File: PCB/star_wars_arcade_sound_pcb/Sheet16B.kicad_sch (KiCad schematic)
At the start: 0 parts

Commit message: Finished schematic
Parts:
- added A_3: LM556, symbol atari:LM556
- added B_2, C_3: TL084, symbol atari:TL084
- added B_3: R5106, symbol atari:R5106
- added C43, C45, C54, C55, C59, C60: .1uf, symbol Device:C
- added C44: .01uf, symbol Device:C
- added C46, C48, C49, C50, C56, C57, C58: .0027uf, symbol Device:C
- added C47, C53: 100uf 50v, symbol Device:C_Polarized_US
- added C51: .47uf, symbol Device:C
- added C52: 10uf 35v, symbol Device:C_Polarized_US
- added Q4: 2N3904, Package_TO_SOT_THT:TO-92_Inline, symbol Transistor_BJT:2N3904
- added R31, R32: 560k, symbol Device:R_US
- added R33, R34: 4.7k, symbol Device:R_US
- added R35, R51, R56: 2.2k, symbol Device:R_US
- added R36: 15, symbol Device:R_US
- added R37: 10k, symbol Device:R_US
- added R38: 470, symbol Device:R_US
- added R39, R40, R42, R46, R47: 12k, symbol Device:R_US
- added R41: 68k, symbol Device:R_US
- added R43: 1.5k, symbol Device:R_US
- added R44: 100, symbol Device:R_US
- added R45: 470k, symbol Device:R_US
- added R48, R49, R52, R53: 22k, symbol Device:R_US
- added R50, R54, R55: 47k, symbol Device:R_US
- added TP10, TP8, TP9: tp_2_pin, symbol atari:tp_2_pin
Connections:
- new net: B_2.1, B_2.2 (-), C56.2, C57.2, R48.1, R52.1
- new net: B_2.6 (-), R48.2, R49.2, R50.1
- new net: Q4.2 (B), R37.2
- new net: Q4.3 (C), R36.1
- new net: B_2.9 (-), R52.2, R55.1
- new net: B_2.8, R55.2, R56.1, TP10.1, TP10.2
- new net: R41.1, R42.2, R43.1
- new net: B_3.5 (VBB), C52.1, R43.2
- new net: A_3.2 (THR), A_3.6 (TR), B_2.12 (+), C43.2, R32.1
- new net: A_3.1 (DIS), R31.1, R32.2
- new net: B_2.10 (+), R53.2, R54.2
- new net: C50.2, C_3.12 (+), R40.2
- new net: B_2.7, R50.2, R51.1, TP9.1, TP9.2
- new net: B_3.8 (VDD), C53.1, C54.1, R44.1
- new net: C56.1, C57.1, R46.2, R47.1
- new net: B_2.3 (+), C58.2, R47.2
- new net: C48.1, C49.1, R39.2, R40.1
- new net: A_3.3 (CV), C44.2
- new net: A_3.13 (DIS), R33.1, R34.2
- new net: B_3.4 (OUT), C55.1
- new net: C55.2, C_3.10 (+), R45.2
- new net: A_3.11 (CV), C47.1
- new net: A_3.12 (THR), A_3.8 (TR), C46.2, R34.1
- new net: C47.2, R35.2, R36.2, R38.2
- new net: B_3.6 (IN), C51.2, R41.2
- new net: B_2.13 (-), B_2.14, R35.1
- new net: C_3.8, C_3.9 (-), R46.1
- new net +12V: A_3.10 (R), A_3.14 (VCC), A_3.4 (R), B_2.4 (V+), C45.1, C59.1, R31.2, R33.2, R44.2
- new net -5V: B_2.11 (V-), C60.1
- new net AUD: C48.2, C49.2, C51.1, C_3.13 (-), C_3.14, R49.1, R53.1, TP8.1, TP8.2
- new net GND: A_3.7 (GND), B_2.5 (+), B_3.2 (VSS), B_3.7 (SYNC), C43.1, C44.1, C45.2, C46.1, C50.1, C52.2, C53.2, C54.2, C58.1, C59.2, C60.2, Q4.1 (E), R38.1, R42.1, R45.1, R54.1
- new net LEFT_AUDIO: R51.2
- new net PA3: R37.1
- new net RCK: A_3.9 (Q), B_3.1 (CLK)
- new net RIGHT_AUDIO: R56.2
- new net SUM: R39.1
- no-connect marks 0 -> 2
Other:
- note added: "DELAY"
- note added: "DELAY CLOCK"
- note added: "FILTER"
- note added: "OUTPUT AND SUMMING AMPLIFIERS"

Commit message: Began PCB layout
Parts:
- B_3: footprint (none) -> atari:DIP8
- Q4: footprint Package_TO_SOT_THT:TO-92_Inline -> (none)
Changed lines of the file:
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@@
       (effects (font (size 1.27 1.27)) (justify left))
     )
-    (property "Footprint" "Package_TO_SOT_THT:TO-92_Inline" (id 2) (at 220.345 218.44 0)
+    (property "Footprint" "" (id 2) (at 220.345 218.44 0)
       (effects (font (size 1.27 1.27) italic) (justify left) hide)
     )
@@
       (effects (font (size 1.27 1.27)) (justify left))
     )
-    (property "Footprint" "" (id 2) (at 135.255 71.755 0)
-      (effects (font (size 1.27 1.27)) hide)
-    )
+    (property "Footprint" "atari:DIP8" (id 2) (at 135.255 71.755 0)
+      (effects (font (size 1.27 1.27)) hide)
+    )

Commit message: ICs placed
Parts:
- A_3, B_2, C_3: footprint (none) -> atari:DIP14
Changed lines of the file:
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@@
       (effects (font (size 1.27 1.27)) (justify left))
     )
-    (property "Footprint" "" (id 2) (at 224.155 60.325 0)
+    (property "Footprint" "atari:DIP14" (id 2) (at 224.155 60.325 0)
       (effects (font (size 1.27 1.27)) hide)
     )
@@
     (property "Reference" "A_3" (id 0) (at 167.64 160.655 0))
     (property "Value" "LM556" (id 1) (at 167.64 162.56 0))
-    (property "Footprint" "" (id 2) (at 167.64 161.29 0)
+    (property "Footprint" "atari:DIP14" (id 2) (at 167.64 161.29 0)
       (effects (font (size 1.27 1.27)) hide)
     )
@@
     (property "Reference" "B_2" (id 0) (at 290.83 92.71 0))
     (property "Value" "TL084" (id 1) (at 290.83 94.615 0))
-    (property "Footprint" "" (id 2) (at 291.465 95.885 0)
+    (property "Footprint" "atari:DIP14" (id 2) (at 291.465 95.885 0)
       (effects (font (size 1.27 1.27)) hide)
     )
@@
     (property "Reference" "B_2" (id 0) (at 290.83 64.77 0))
     (property "Value" "TL084" (id 1) (at 290.83 66.675 0))
-    (property "Footprint" "" (id 2) (at 291.465 67.945 0)
+    (property "Footprint" "atari:DIP14" (id 2) (at 291.465 67.945 0)
       (effects (font (size 1.27 1.27)) hide)
     )
@@
     (property "Reference" "A_3" (id 0) (at 233.68 160.02 0))
     (property "Value" "LM556" (id 1) (at 233.68 161.925 0))
-    (property "Footprint" "" (id 2) (at 233.68 161.29 0)
+    (property "Footprint" "atari:DIP14" (id 2) (at 233.68 161.29 0)
       (effects (font (size 1.27 1.27)) hide)
     )
@@
     (property "Reference" "B_2" (id 0) (at 223.52 62.23 0))
     (property "Value" "TL084" (id 1) (at 223.52 64.135 0))
-    (property "Footprint" "" (id 2) (at 224.155 65.405 0)
+    (property "Footprint" "atari:DIP14" (id 2) (at 224.155 65.405 0)
       (effects (font (size 1.27 1.27)) hide)
     )
@@
     (property "Reference" "C_3" (id 0) (at 67.945 67.31 0))
     (property "Value" "TL084" (id 1) (at 67.945 69.215 0))
-    (property "Footprint" "" (id 2) (at 68.58 70.485 0)
+    (property "Footprint" "atari:DIP14" (id 2) (at 68.58 70.485 0)
       (effects (font (size 1.27 1.27)) hide)
     )
@@
     (property "Reference" "B_2" (id 0) (at 190.5 198.12 0))
     (property "Value" "TL084" (id 1) (at 190.5 200.025 0))
-    (property "Footprint" "" (id 2) (at 191.135 201.93 0)
+    (property "Footprint" "atari:DIP14" (id 2) (at 191.135 201.93 0)
       (effects (font (size 1.27 1.27)) hide)
     )
@@
     (property "Reference" "C_3" (id 0) (at 177.165 66.675 0))
     (property "Value" "TL084" (id 1) (at 177.165 64.77 0))
-    (property "Footprint" "" (id 2) (at 177.8 67.945 0)
-      (effects (font (size 1.27 1.27)) hide)
-    )
+    (property "Footprint" "atari:DIP14" (id 2) (at 177.8 67.945 0)
+      (effects (font (size 1.27 1.27)) hide)
+    )

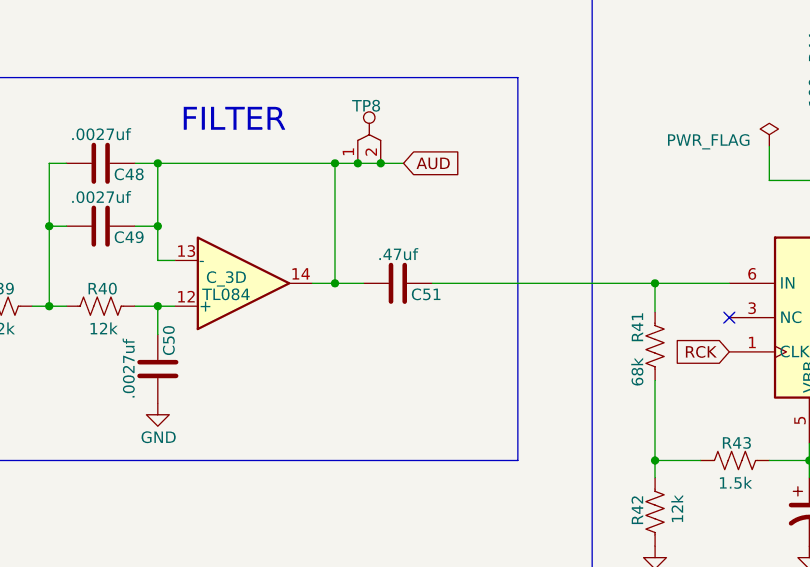
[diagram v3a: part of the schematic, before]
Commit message: Placed all components
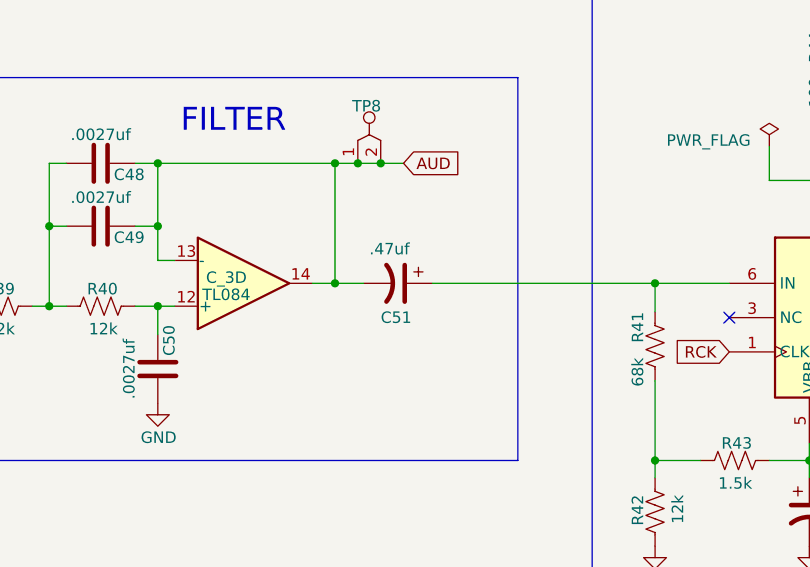
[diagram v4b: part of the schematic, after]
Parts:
- removed C51: .47uf, symbol Device:C
- added C51: .47uf, atari:MedCap1, symbol Device:C_Polarized_US
- C43, C44, C45, C46, C48, C49, C50, C54, C55, C56, C57, C58, C59, C60, R31, R32, R33, R34, R35, R36, R37, R38, R39, R40, R41, R42, R43, R44, R45, R46, R47, R48, R49, R50, R51, R52, R53, R54, R55, R56: footprint (none) -> atari:GenericComp
- C47, C53: footprint (none) -> atari:LargeCap1
- C52: footprint (none) -> atari:MedCap1
- Q4: footprint (none) -> atari:GenericTrans
- TP10, TP8, TP9: footprint (none) -> atari:TEST_POINT
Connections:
- net AUD: now also C51.2
- net at B_3.6 (IN), R41.2: now also C51.1

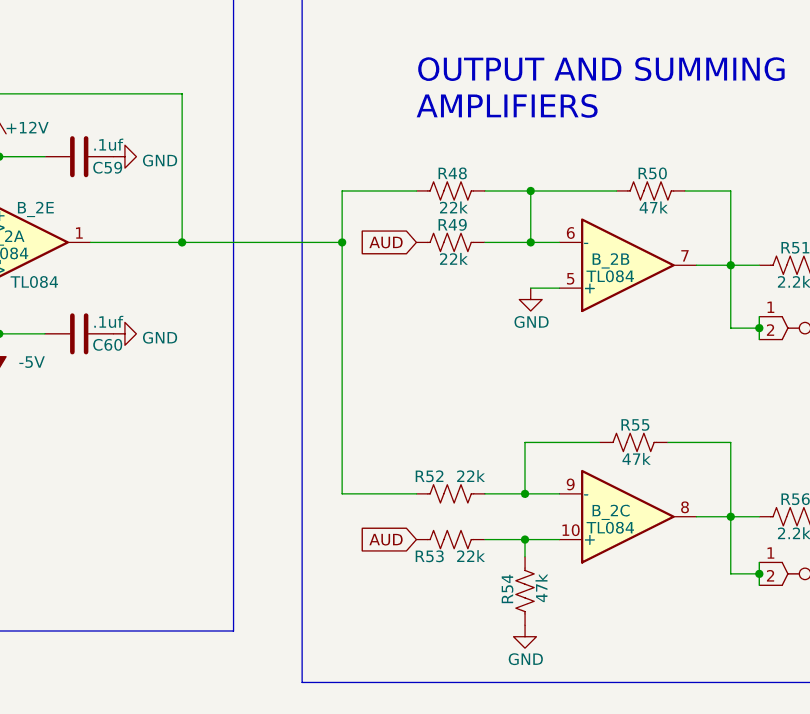
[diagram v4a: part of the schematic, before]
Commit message: Ground plane and mounting holes remain
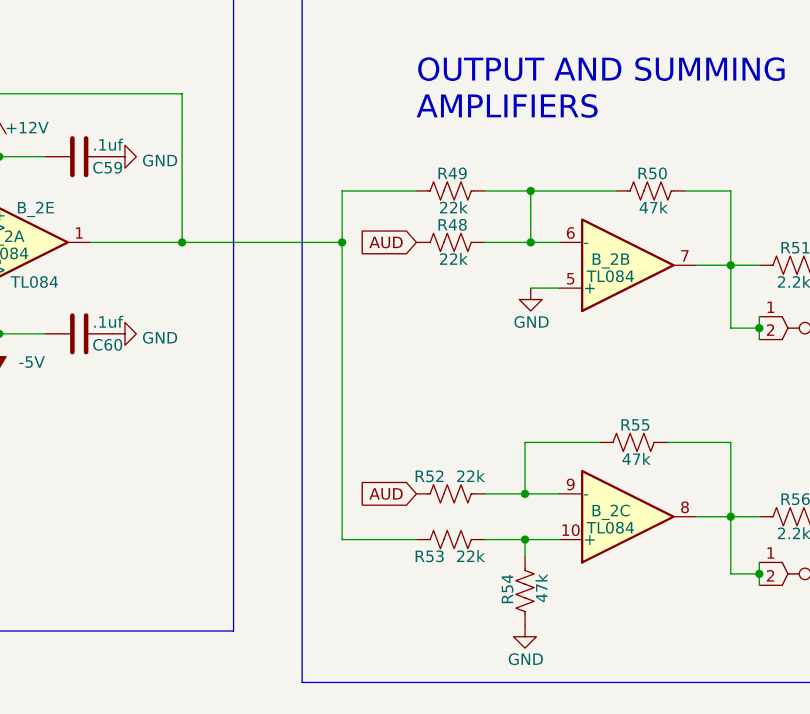
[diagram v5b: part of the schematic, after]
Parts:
- renumbered R49 to R48, R48 to R49
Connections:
- net AUD: now also R52.1; no longer R53.1
- net at B_2.1, B_2.2 (-), C56.2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: now also R53.1; no longer R52.1
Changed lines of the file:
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@@
     (stroke (width 0) (type default) (color 0 0 0 0))
   )
-  (wire (pts (xy 260.985 62.865) (xy 260.985 90.805))
+  (wire (pts (xy 260.985 62.865) (xy 260.985 95.885))
     (stroke (width 0) (type default) (color 0 0 0 0))
   )
@@
     (stroke (width 0) (type default) (color 0 0 0 0))
   )
-  (wire (pts (xy 260.985 90.805) (xy 269.24 90.805))
-    (stroke (width 0) (type default) (color 0 0 0 0))
-  )
   (wire (pts (xy 229.87 199.39) (xy 229.87 201.295))
     (stroke (width 0) (type default) (color 0 0 0 0))
@@
   )
   (wire (pts (xy 172.085 149.225) (xy 163.195 149.225))
+    (stroke (width 0) (type default) (color 0 0 0 0))
+  )
+  (wire (pts (xy 269.24 95.885) (xy 260.985 95.885))
     (stroke (width 0) (type default) (color 0 0 0 0))
   )
@@
     )
   )
-  (global_label "AUD" (shape input) (at 269.24 95.885 180) (fields_autoplaced)
+  (global_label "AUD" (shape input) (at 269.24 90.805 180) (fields_autoplaced)
     (effects (font (size 1.27 1.27)) (justify right))
-    (property "Intersheet References" "${INTERSHEET_REFS}" (id 0) (at 263.1379 95.8056 0)
+    (property "Intersheet References" "${INTERSHEET_REFS}" (id 0) (at 263.1379 90.7256 0)
       (effects (font (size 1.27 1.27)) (justify right) hide)
     )
@@
   (symbol (lib_id "Device:R_US") (at 273.05 57.15 90) (unit 1)
     (in_bom yes) (on_board yes)
-    (property "Reference" "R48" (id 0) (at 274.955 55.245 90)
+    (property "Reference" "R49" (id 0) (at 274.955 55.245 90)
       (effects (font (size 1.27 1.27)) (justify left))
     )
@@
   (symbol (lib_id "Device:R_US") (at 273.05 62.865 90) (unit 1)
     (in_bom yes) (on_board yes)
-    (property "Reference" "R49" (id 0) (at 274.955 60.96 90)
-      (effects (font (size 1.27 1.27)) (justify left))
-    )
+    (property "Reference" "R48" (id 0) (at 274.955 60.96 90)
+      (effects (font (size 1.27 1.27)) (justify left))
+    )

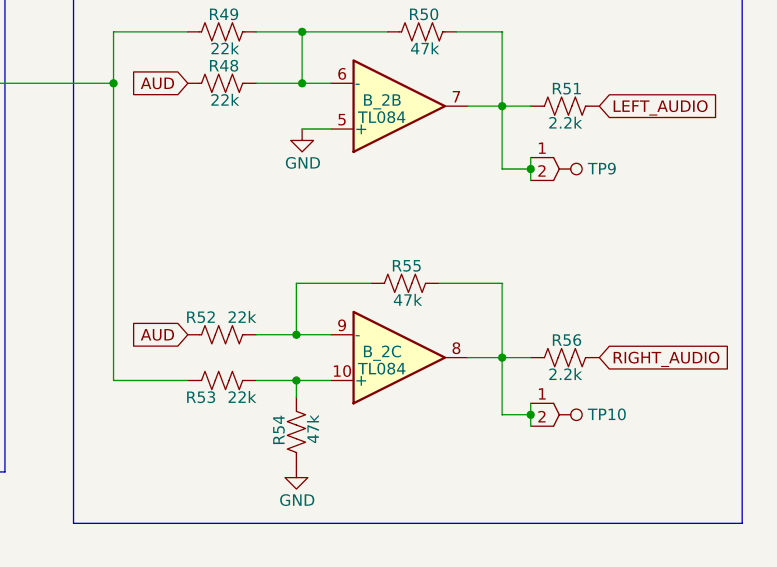
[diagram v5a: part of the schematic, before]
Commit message: Bottom keep out areas remain
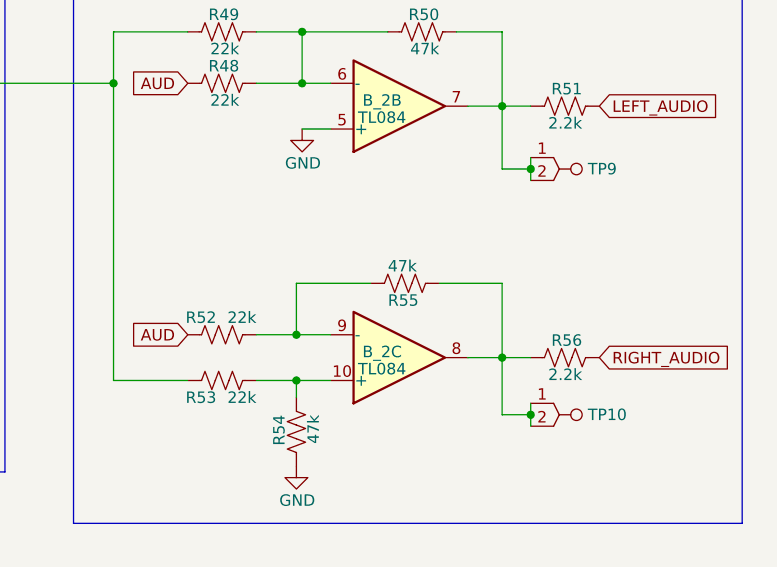
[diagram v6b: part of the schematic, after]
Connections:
- net at B_2.9 (-), R52.2: now also R55.2; no longer R55.1
- net at B_2.8, R56.1, TP10.1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: now also R55.1; no longer R55.2
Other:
- moved on the sheet: R55
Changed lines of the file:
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@@
     (pin "3")
   )
-  (symbol (lib_id "Device:R_US") (at 293.37 85.09 90) (unit 1)
+  (symbol (lib_id "Device:R_US") (at 293.37 85.09 270) (unit 1)
     (in_bom yes) (on_board yes)
-    (property "Reference" "R55" (id 0) (at 295.275 83.185 90)
+    (property "Reference" "R55" (id 0) (at 291.465 86.995 90)
       (effects (font (size 1.27 1.27)) (justify left))
     )
-    (property "Value" "47k" (id 1) (at 295.275 86.995 90)
+    (property "Value" "47k" (id 1) (at 291.465 83.185 90)
       (effects (font (size 1.27 1.27)) (justify left))
     )
-    (property "Footprint" "atari:GenericComp" (id 2) (at 293.624 84.074 90)
+    (property "Footprint" "atari:GenericComp" (id 2) (at 293.116 86.106 90)
       (effects (font (size 1.27 1.27)) hide)
     )
